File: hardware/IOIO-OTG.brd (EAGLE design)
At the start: 68.6 x 30.5 mm, 60 parts, among them Q1 IRLML2244, Q2 2N7002PW, Q3 AO3404A, U1 PIC24FJ256GB206, U14 SWITCH_SPDT, U2 TPS62133RGTT, U3 VREG_MIC5216

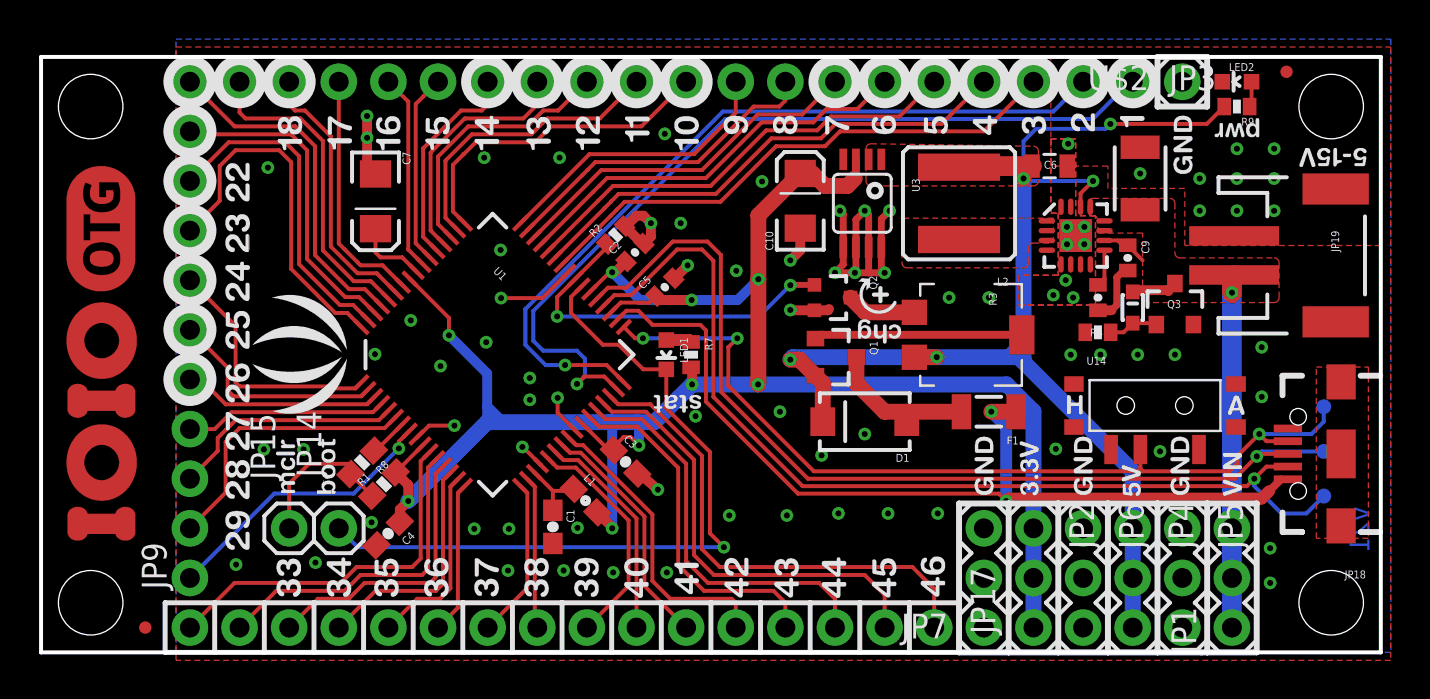
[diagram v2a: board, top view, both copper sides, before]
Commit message: All remaining 0402 passives bumped to 0603
all components had slight shift in X/Y coordinates. Components near the
TPS6124 also requires some shifting. Included an "original" and "moved
to 0603" screen shot of design for review.
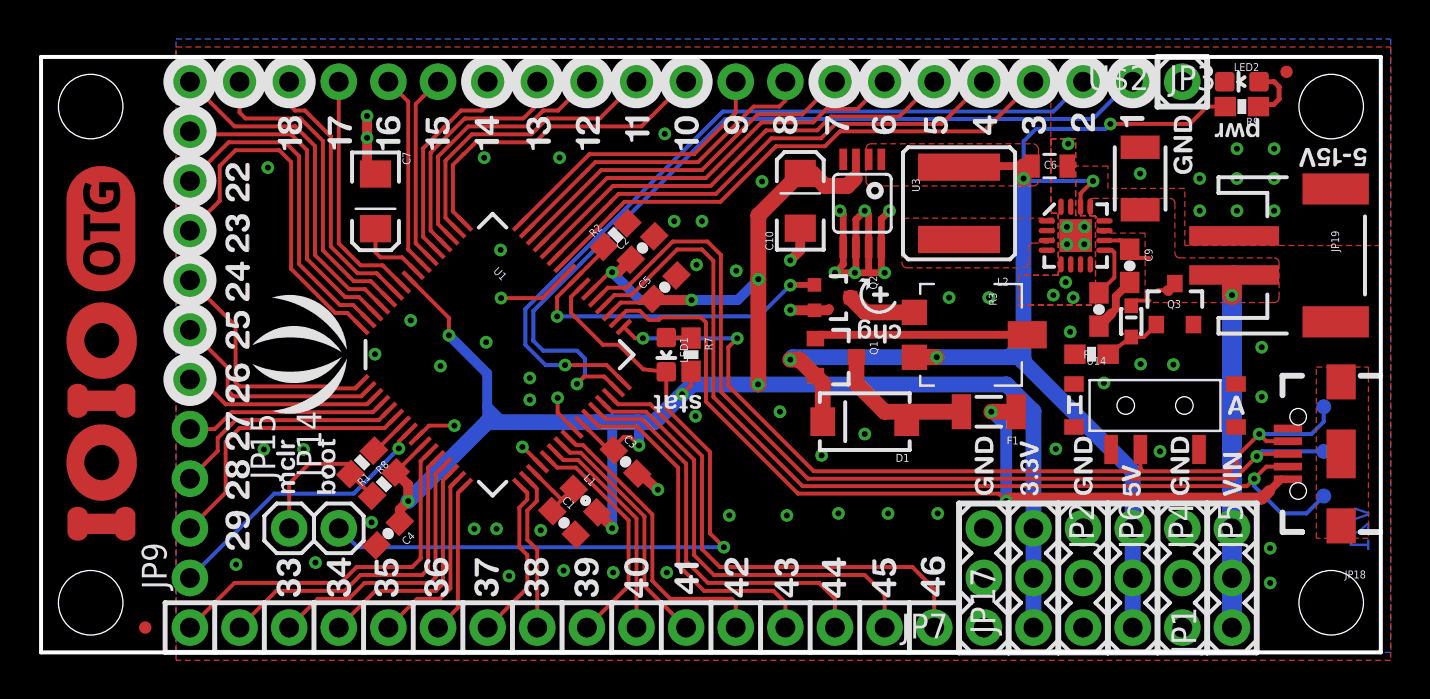
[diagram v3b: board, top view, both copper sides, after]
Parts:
- C2, C5, C8, C9: device SparkFun:0402-CAP -> SparkFun-Capacitors:0603-CAP
- LED1: value LY L29K-J1K2-26-Z -> Yellow; device SparkFun:LED-0603 -> SparkFun-LED:LED-0603
- LED2: value LS L29K-G1J2-1-Z -> RED; device SparkFun:LED-0603 -> SparkFun-LED:LED-0603
- R2, R4: device SparkFun:0402-RES -> SparkFun-Resistors:0603-RES
- R3: device SparkFun-Electromechanical:TRIMPOT-5MM -> SparkFun-Electromechanical:TRIMPOT_5MM
- R7: value 750 -> 330; device SparkFun:0402-RES -> SparkFun-Resistors:0603-RES
- R9: value 1.6k -> 330; device SparkFun:0402-RES -> SparkFun-Resistors:0603-RES
- moved R4 1.17 mm to (53.8, 15.3)
- moved D2 0.72 mm to (55.8, 16.9)
- moved C8 0.61 mm to (54.2, 17.6)
- moved C1 0.61 mm to (26.8, 6.63), turned to 315 degrees
- moved C2 0.44 mm to (30.8, 20.7)
- moved C9 0.42 mm to (55.7, 19.8)
- moved LED2 0.25 mm to (61.5, 29.2)
- moved R9 0.25 mm to (61.5, 27.9)
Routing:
- net GND: track 42.8 -> 37.4 mm
- net N$3: track 1.31 -> 3.66 mm
- net N$7: track 1.91 -> 3.23 mm
- net 3.3V: track 109.2 -> 110.0 mm
- net N$12: track 2.56 -> 3.12 mm
